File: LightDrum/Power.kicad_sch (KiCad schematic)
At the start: 65 parts, among them U2 AP3401, U3 LM22673-5V, U4 TPS7A94, U5 INA4181 A2, U6 INA4181 A2

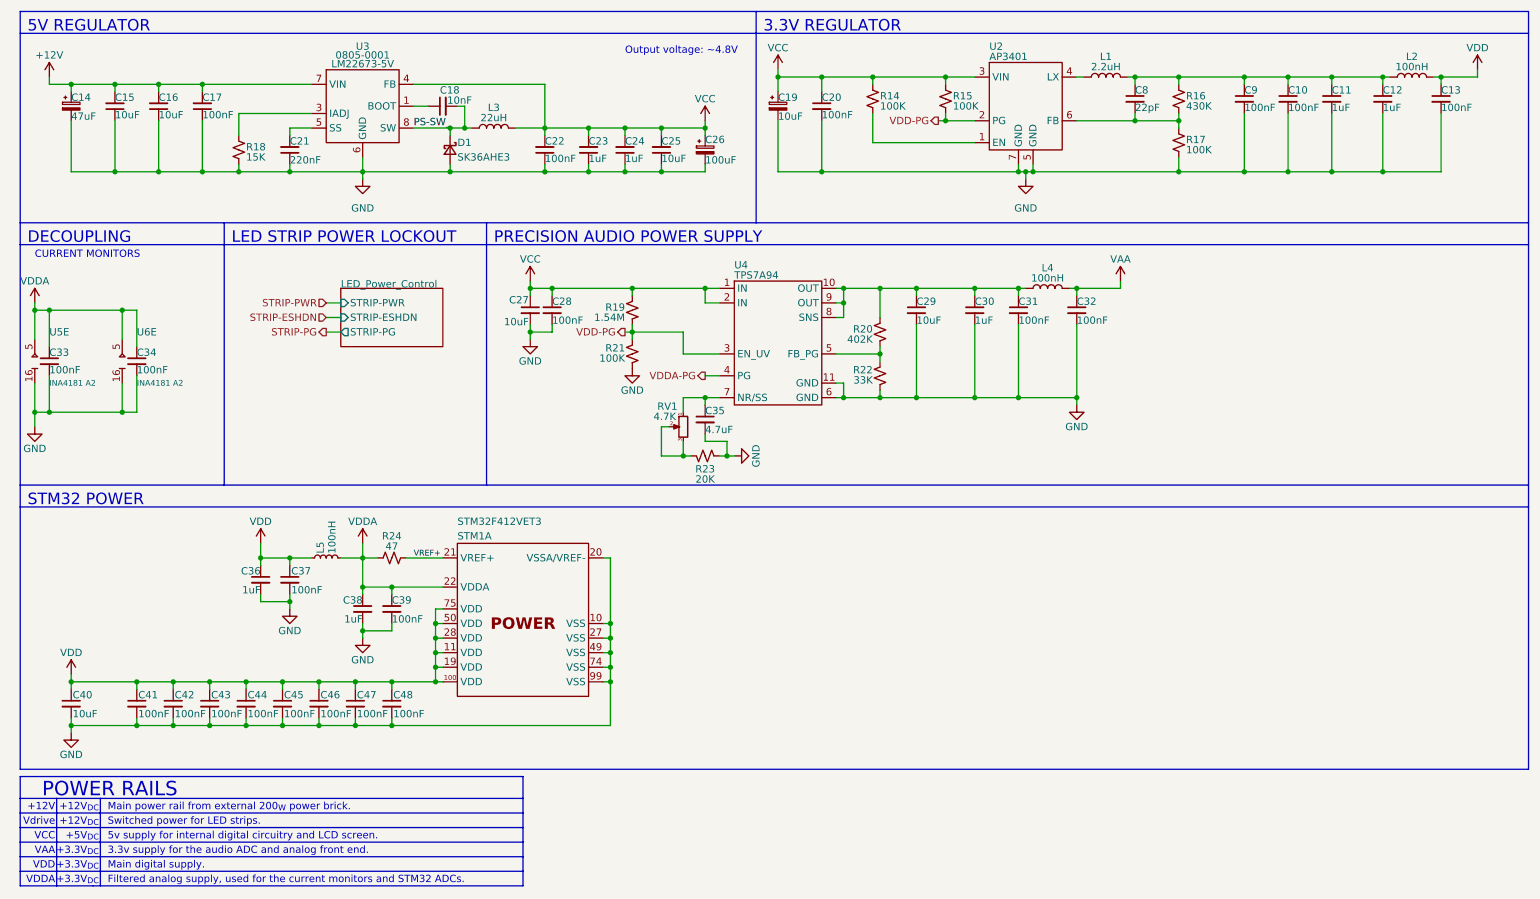
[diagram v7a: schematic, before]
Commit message: Organize old files and generate interface gerbers
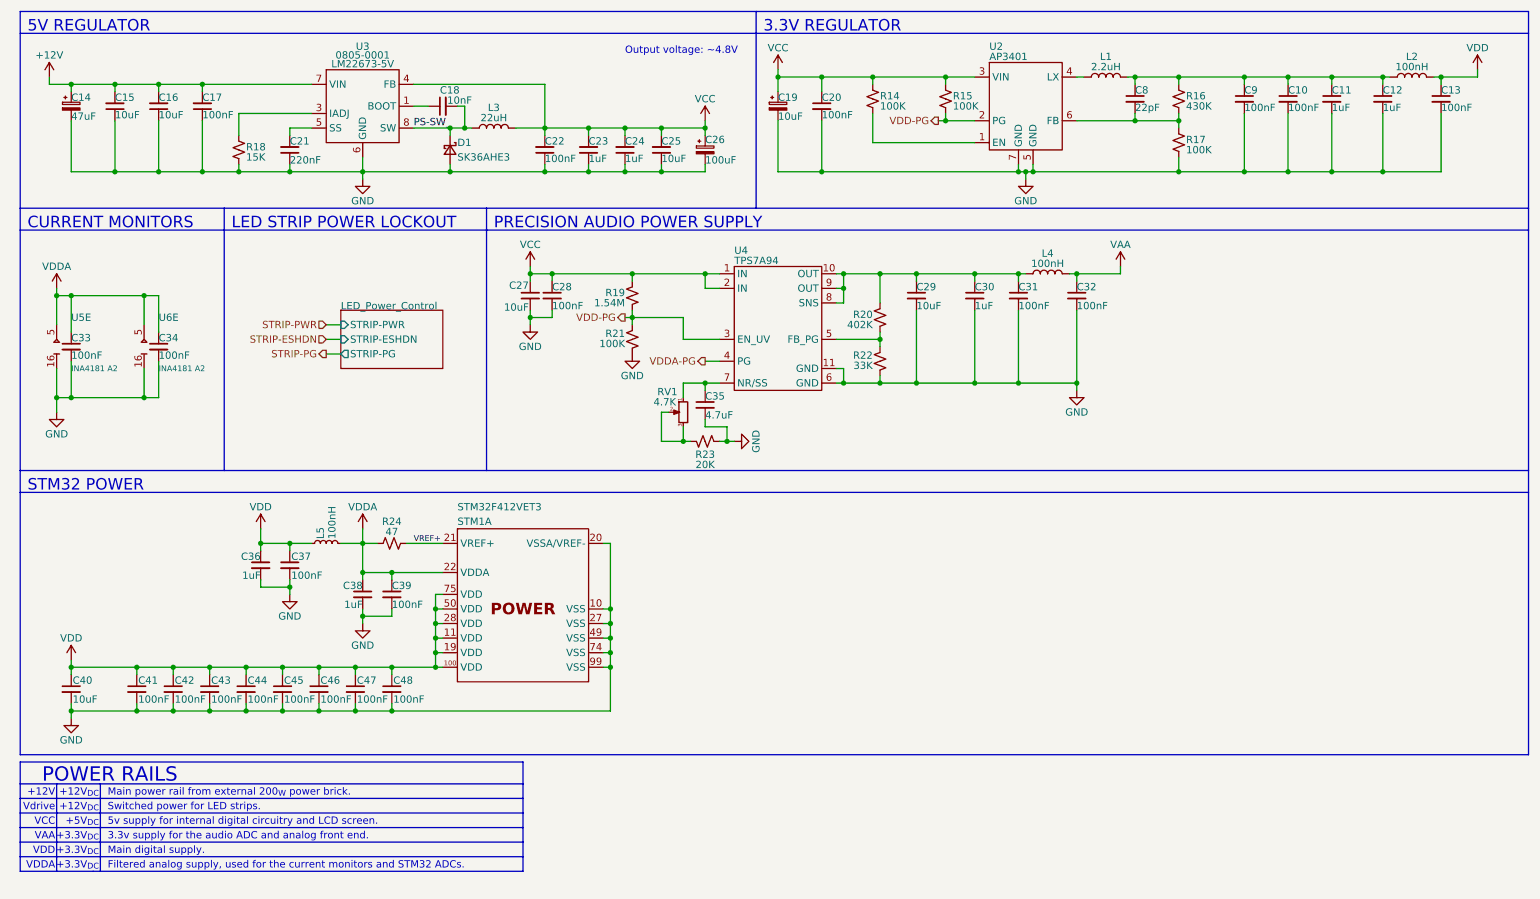
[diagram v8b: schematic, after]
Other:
- note removed: "DECOUPLING"
- moved on the sheet: C27, C28, C29, C30, C31, C32, C33, C34, C35, C36, C37, C38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
